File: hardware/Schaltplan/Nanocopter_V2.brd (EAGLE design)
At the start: 100 x 100 mm, 89 parts, among them M1+ TPTP15SQ, M1- TPTP15SQ, M2+ TPTP15SQ, M2- TPTP15SQ, M3+ TPTP15SQ, M3- TPTP15SQ, M4+ TPTP15SQ, M4- TPTP15SQ, T1 IRLML2502, T2 IRLML2502, T3 IRLML2502, T4 IRLML2502, U2 PRTR5V0U2X, U3 LM3480-3.3, X1 USBSMD

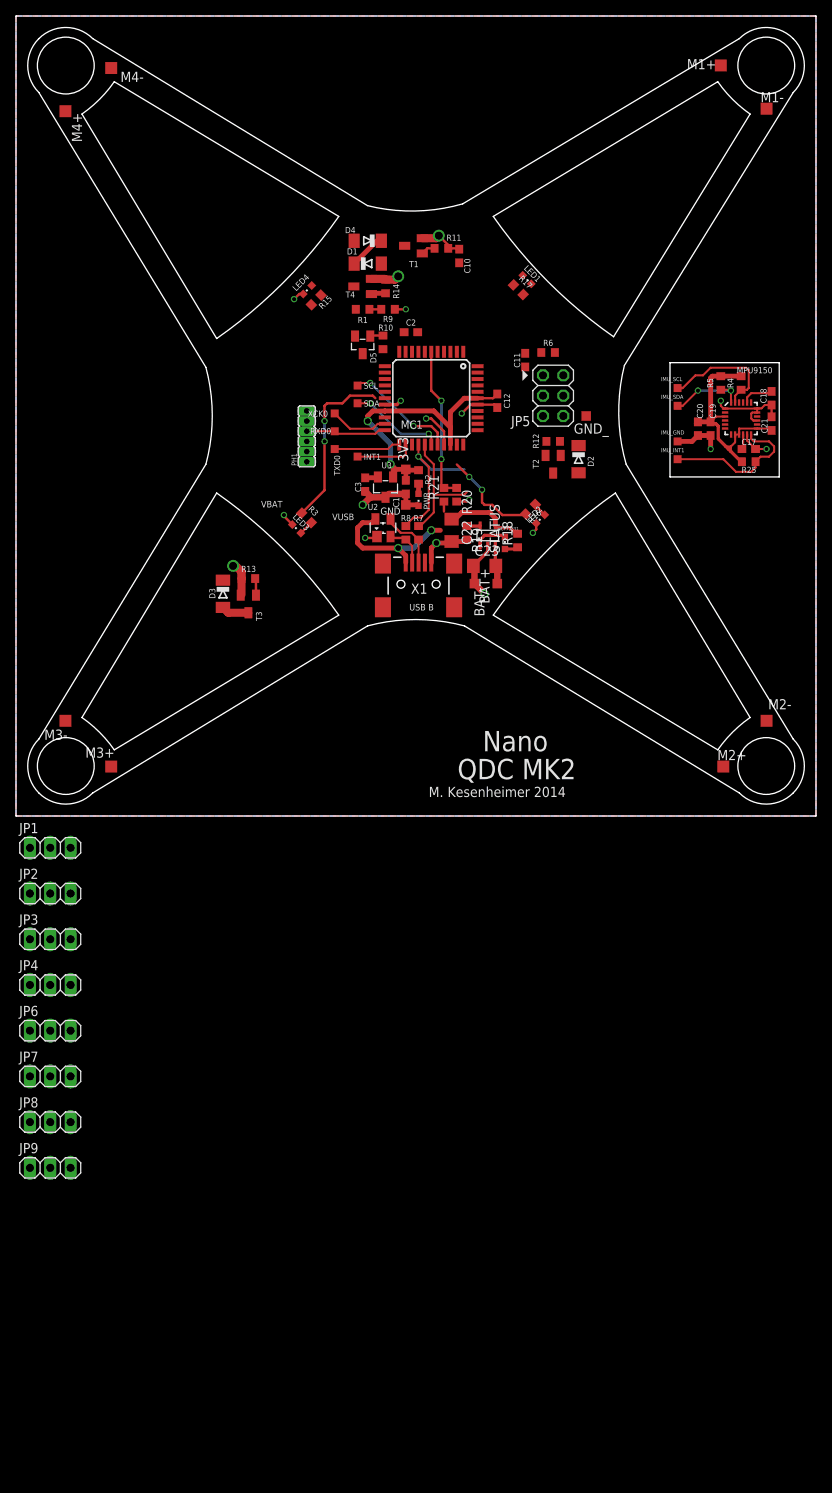
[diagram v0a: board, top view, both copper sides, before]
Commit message: Neuer Schaltplan V2.1. Die Schaltung wird jetzt in zwei Teile aufgeteilt: Flugcontroller (SimpleControl) und Motortreiber-platine (BaseFrame).
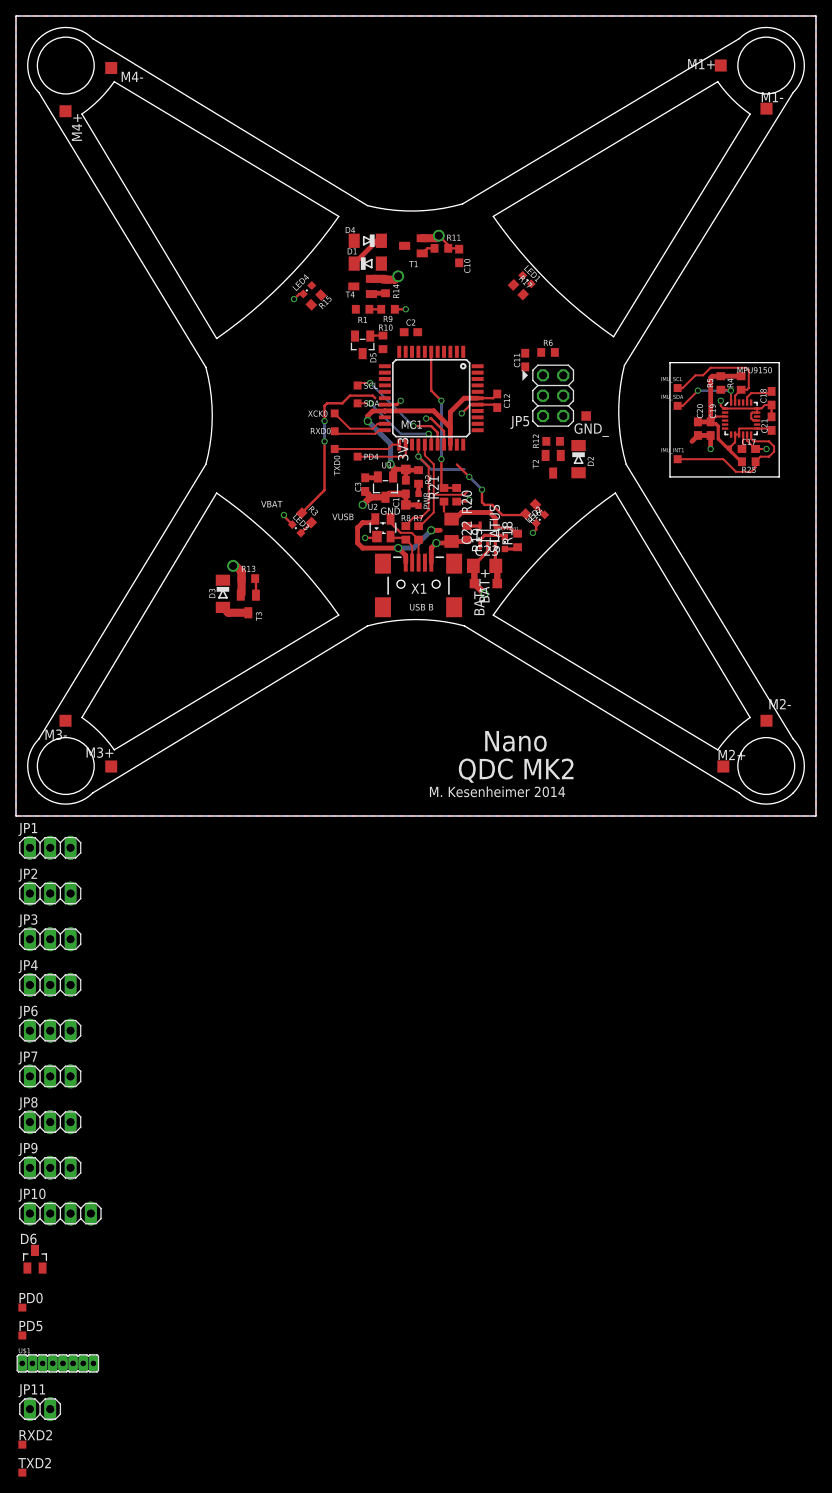
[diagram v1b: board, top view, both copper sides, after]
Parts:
- removed IMU_GND: TPTP10SQ, testpad:TP10SQ
- removed PH1: PH1X6-05LONG, pel_hdr:PHL005-1-6
- added D6: BAT54C, diode:SOT23
- added JP10: (no value), pinhead:1X04
- added JP11: (no value), pinhead:1X02
- added PD0, PD5, RXD2, TXD2: TPTP10SQ, testpad:TP10SQ
- added U$1: PH1X8, pel_hdr:PHL005-1-8
- renumbered INT1 to PD4
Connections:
- removed net +5V: PH1.6
- new net N$6: C3.1, D6.3, U3.2
- new net PD0: MC1.20, PD0.TP, U$1.2
- new net PD4: MC1.24, PD4.TP, U$1.7
- new net PD5: MC1.25, PD5.TP, U$1.8
- new net RXD2: MC1.32, RXD2.TP
- new net TXD2: MC1.33, TXD2.TP
- net BUSYLED1: now also JP10.1
- net BUSYLED2: now also JP10.2
- net BUSYLED3: now also JP10.3
- net BUSYLED4: now also JP10.4
- net GND: now also JP11.1, U$1.1; no longer IMU_GND.TP, PH1.1
- net INT1: no longer MC1.24, PD4.TP
- net RXD0: now also U$1.4; no longer PH1.4
- net TXD0: now also U$1.5
- net V+: now also D6.1
- net VCC: now also D6.2, JP11.2, U$1.6; no longer C3.1, U3.2
- net XCK0: now also U$1.3
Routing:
- net PD4: track 0.00 -> 7.36 mm
- net INT1: track 26.0 -> 18.6 mm
- net RXD0: track 10.1 -> 6.58 mm
- net GND: track 80.2 -> 78.4 mm
- net VCC: track 6.37 -> 4.74 mm
- net N$6: track 0.00 -> 1.63 mm
